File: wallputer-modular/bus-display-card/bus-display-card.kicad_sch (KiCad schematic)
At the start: 1 part

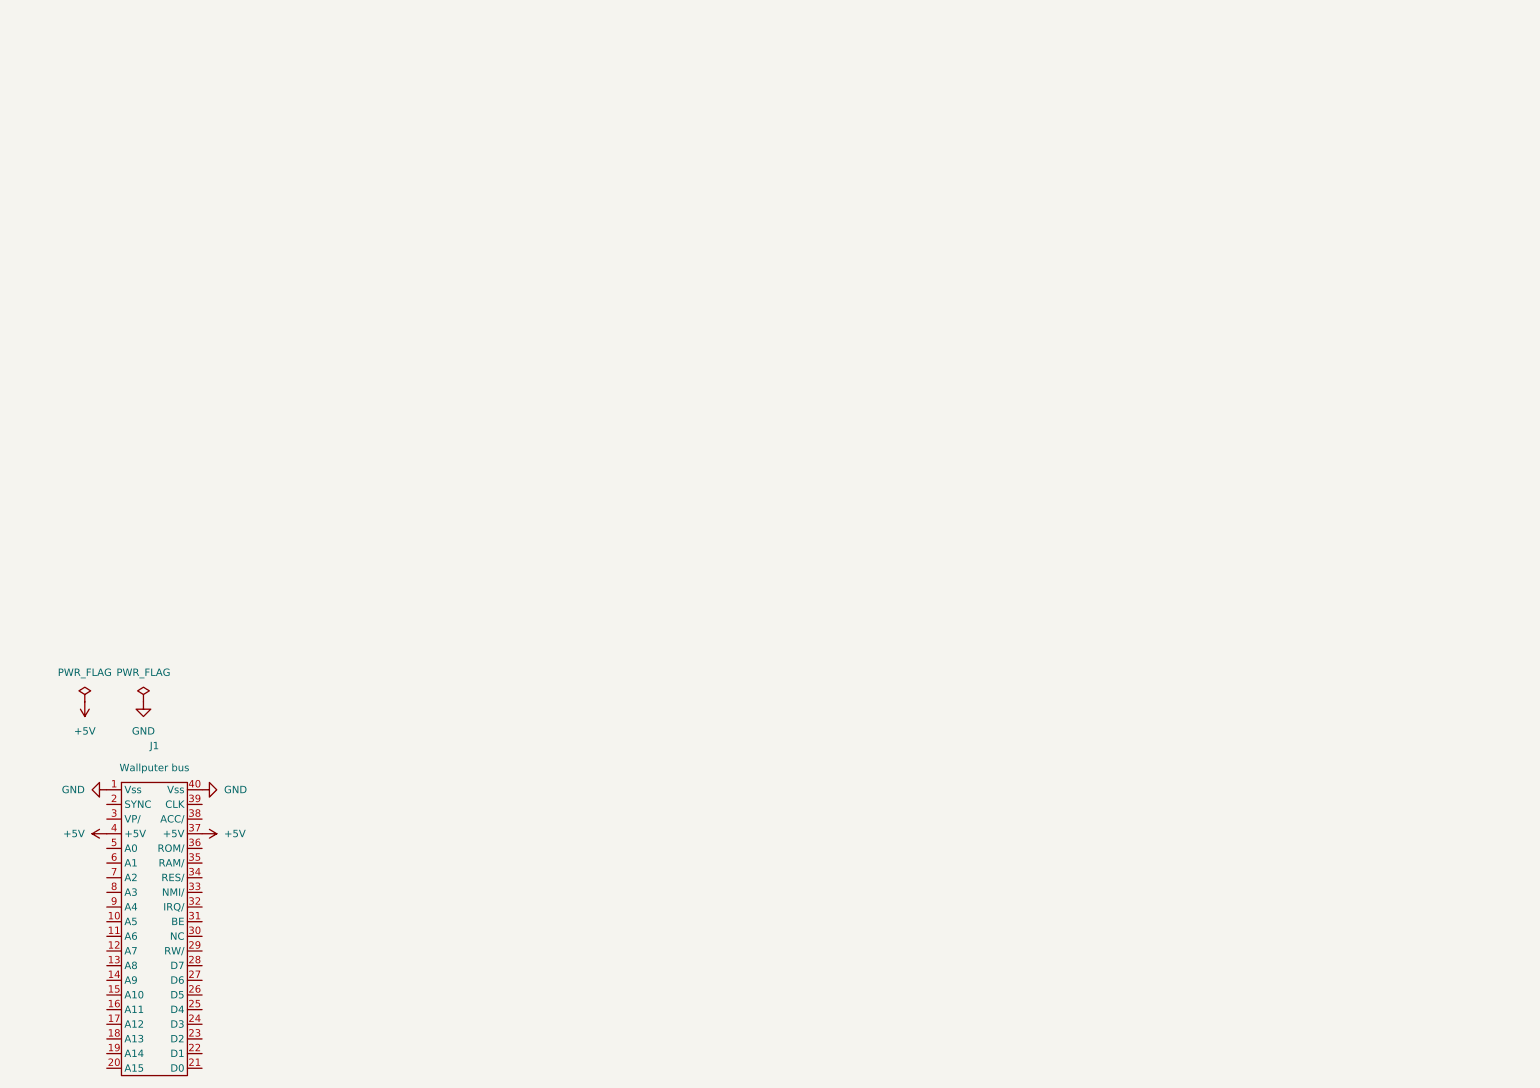
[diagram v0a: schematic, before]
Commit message: copy parts of single board
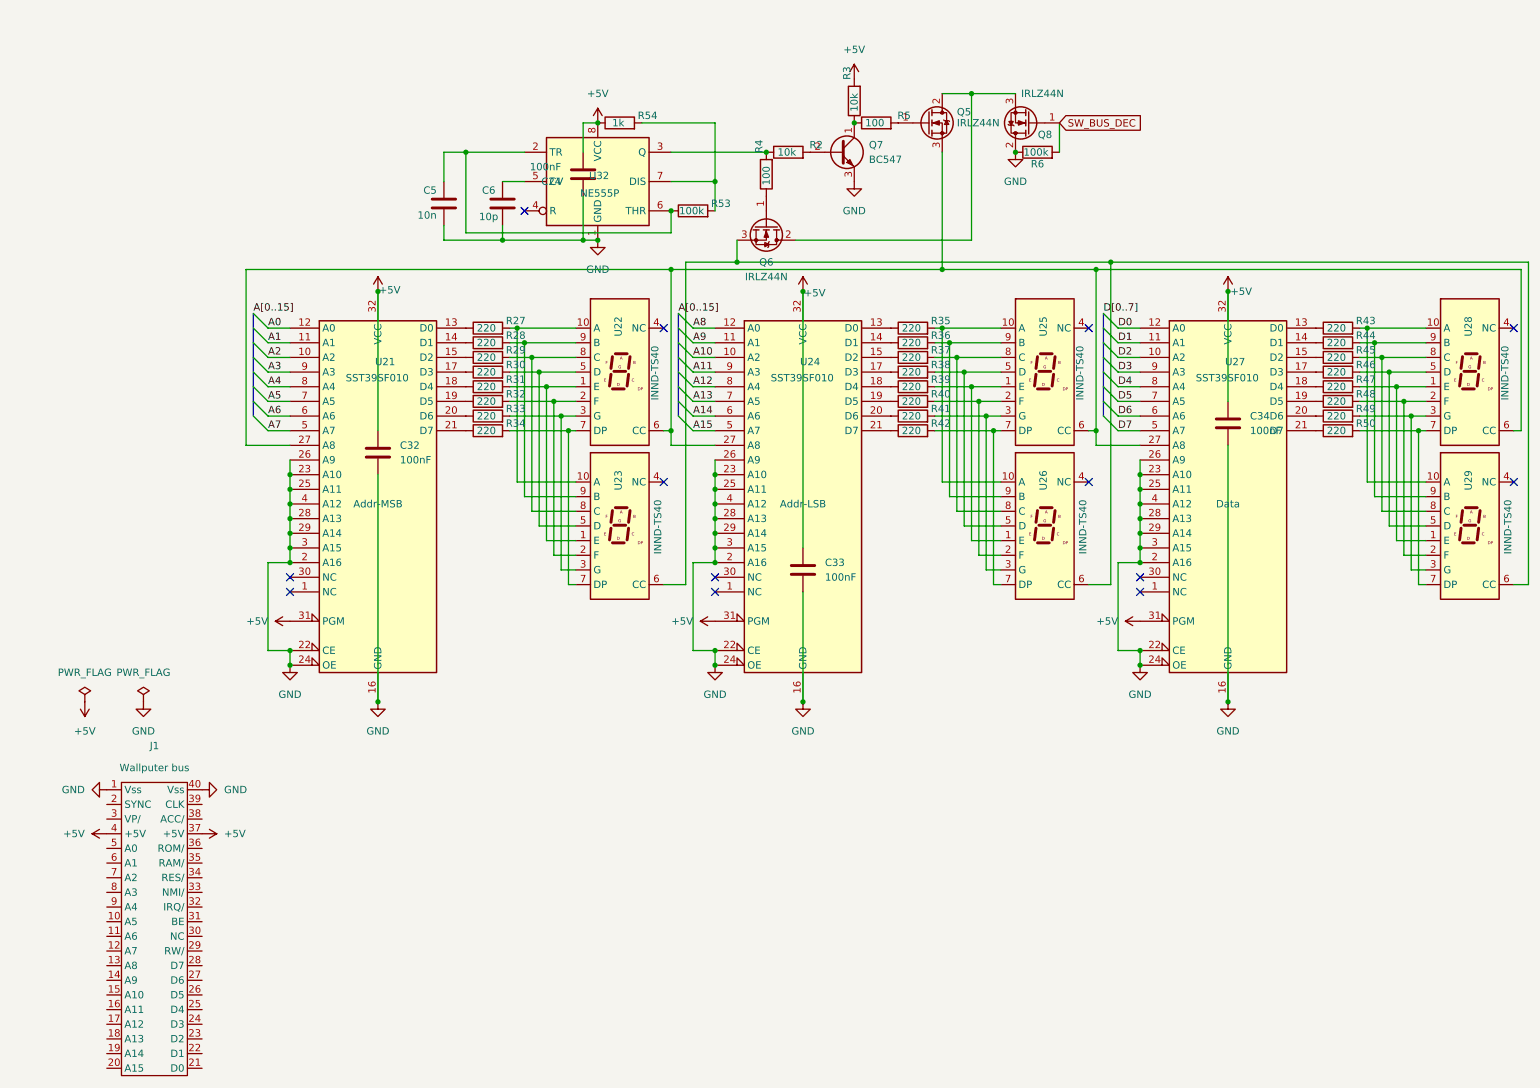
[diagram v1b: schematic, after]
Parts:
- added C24, C32, C33, C34: 100nF, Capacitor_THT:C_Disc_D5.0mm_W2.5mm_P5.00mm, symbol Device:C
- added C5: 10n, Capacitor_THT:C_Disc_D5.0mm_W2.5mm_P5.00mm, symbol Device:C
- added C6: 10p, Capacitor_THT:C_Disc_D5.0mm_W2.5mm_P5.00mm, symbol Device:C
- added Q5, Q6, Q8: IRLZ44N, Package_TO_SOT_THT:TO-220-3_Vertical, symbol Transistor_FET:IRLZ44N
- added Q7: BC547, Package_TO_SOT_THT:TO-92_Inline, symbol Transistor_BJT:BC547
- added R2, R3: 10k, Resistor_THT:R_Axial_DIN0204_L3.6mm_D1.6mm_P2.54mm_Vertical, symbol Device:R
- added R27, R28, R29, R30, R31, R32, R33, R34, R35, R36, R37, R38, R39, R40, R41, R42, R43, R44, R45, R46, R47, R48, R49, R50: 220, Resistor_THT:R_Axial_DIN0204_L3.6mm_D1.6mm_P2.54mm_Vertical, symbol Device:R
- added R4, R5: 100, Resistor_THT:R_Axial_DIN0204_L3.6mm_D1.6mm_P2.54mm_Vertical, symbol Device:R
- added R53, R6: 100k, Resistor_THT:R_Axial_DIN0204_L3.6mm_D1.6mm_P2.54mm_Vertical, symbol Device:R
- added R54: 1k, Resistor_THT:R_Axial_DIN0204_L3.6mm_D1.6mm_P2.54mm_Vertical, symbol Device:R
- added U21, U24, U27: SST39SF010, Package_DIP:DIP-32_W15.24mm_Socket, symbol Memory_Flash:SST39SF010
- added U22, U23, U25, U26, U28, U29: INND-TS40, wallputer:INND-TS40, symbol New_Library:INND-TS40_1
- added U32: NE555P, Package_DIP:DIP-8_W7.62mm, symbol Timer:NE555P
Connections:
- net +5V: now also C24.2, C32.1, C33.1, C34.1, R3.2, R54.1, U21.31 (PGM), U21.32 (VCC), U24.31 (PGM), U24.32 (VCC), U27.31 (PGM), U27.32 (VCC), U32.8 (VCC)
- net GND: now also C24.1, C32.2, C33.2, C34.2, C5.2, C6.2, Q7.3 (E), Q8.2 (D), R6.1, U21.16 (GND), U21.2 (A16), U21.22 (CE), U21.23 (A10), U21.24 (OE), U21.25 (A11), U21.26 (A9), U21.28 (A13), U21.29 (A14), U21.3 (A15), U21.4 (A12), U24.16 (GND), U24.2 (A16), U24.22 (CE), U24.23 (A10), U24.24 (OE), U24.25 (A11), U24.26 (A9), U24.28 (A13), U24.29 (A14), U24.3 (A15), U24.4 (A12), U27.16 (GND), U27.2 (A16), U27.22 (CE), U27.23 (A10), U27.24 (OE), U27.25 (A11), U27.26 (A9), U27.28 (A13), U27.29 (A14), U27.3 (A15), U27.4 (A12), U32.1 (GND)
- new net: R37.1, U24.15 (D2)
- new net: R37.2, U25.8 (C), U26.8 (C)
- new net: R39.2, U25.1 (E), U26.1 (E)
- new net: R35.2, U25.10 (A), U26.10 (A)
- new net: R40.2, U25.2 (F), U26.2 (F)
- new net: R41.2, U25.3 (G), U26.3 (G)
- new net: R38.2, U25.5 (D), U26.5 (D)
- new net: Q5.3 (S), U21.27 (A8), U22.6 (CC), U24.27 (A8), U25.6 (CC), U27.27 (A8), U28.6 (CC)
- new net: R42.2, U25.7 (DP), U26.7 (DP)
- new net: R36.2, U25.9 (B), U26.9 (B)
- new net: R43.1, U27.13 (D0)
- new net: R44.1, U27.14 (D1)
- new net: R45.1, U27.15 (D2)
- new net: R46.1, U27.17 (D3)
- new net: R47.1, U27.18 (D4)
- new net: R48.1, U27.19 (D5)
- new net: R49.1, U27.20 (D6)
- new net: R50.1, U27.21 (D7)
- new net: R33.1, U21.20 (D6)
- new net: R33.2, U22.3 (G), U23.3 (G)
- new net: R38.1, U24.17 (D3)
- new net: R34.1, U21.21 (D7)
- new net: R34.2, U22.7 (DP), U23.7 (DP)
- new net: R47.2, U28.1 (E), U29.1 (E)
- new net: R43.2, U28.10 (A), U29.10 (A)
- new net: R48.2, U28.2 (F), U29.2 (F)
- new net: R49.2, U28.3 (G), U29.3 (G)
- new net: R46.2, U28.5 (D), U29.5 (D)
- new net: R50.2, U28.7 (DP), U29.7 (DP)
- new net: R45.2, U28.8 (C), U29.8 (C)
- new net: R44.2, U28.9 (B), U29.9 (B)
- new net: Q6.1 (G), R4.1
- new net: Q5.2 (D), Q6.2 (D), Q8.3 (S)
- new net: Q6.3 (S), U23.6 (CC), U26.6 (CC), U29.6 (CC)
- new net: R53.2, R54.2, U32.7 (DIS)
- new net: Q7.1 (C), R3.1, R5.1
- new net: Q7.2 (B), R2.2
- new net: R28.1, U21.14 (D1)
- new net: R28.2, U22.9 (B), U23.9 (B)
- new net: R39.1, U24.18 (D4)
- new net: R36.1, U24.14 (D1)
- new net: R2.1, R4.2, U32.3 (Q)
- new net: R31.2, U22.1 (E), U23.1 (E)
- new net: R27.2, U22.10 (A), U23.10 (A)
- new net: R32.2, U22.2 (F), U23.2 (F)
- new net: R30.2, U22.5 (D), U23.5 (D)
- new net: R29.2, U22.8 (C), U23.8 (C)
- new net: R27.1, U21.13 (D0)
- new net: R29.1, U21.15 (D2)
- new net: R30.1, U21.17 (D3)
- new net: R31.1, U21.18 (D4)
- new net: R32.1, U21.19 (D5)
- new net: R35.1, U24.13 (D0)
- new net: R40.1, U24.19 (D5)
- new net: R41.1, U24.20 (D6)
- new net: R42.1, U24.21 (D7)
- new net: Q5.1 (G), R5.2
- new net: C5.1, R53.1, U32.2 (TR), U32.6 (THR)
- new net: C6.1, U32.5 (CV)
- new net A0: U21.12 (A0)
- new net A1: U21.11 (A1)
- new net A10: U24.10 (A2)
- new net A11: U24.9 (A3)
- new net A12: U24.8 (A4)
- new net A13: U24.7 (A5)
- new net A14: U24.6 (A6)
- new net A15: U24.5 (A7)
- new net A2: U21.10 (A2)
- new net A3: U21.9 (A3)
- new net A4: U21.8 (A4)
- new net A5: U21.7 (A5)
- new net A6: U21.6 (A6)
- new net A7: U21.5 (A7)
- new net A8: U24.12 (A0)
- new net A9: U24.11 (A1)
- new net D0: U27.12 (A0)
- new net D1: U27.11 (A1)
- new net D2: U27.10 (A2)
- new net D3: U27.9 (A3)
- new net D4: U27.8 (A4)
- new net D5: U27.7 (A5)
- new net D6: U27.6 (A6)
- new net D7: U27.5 (A7)
- new net SW_BUS_DEC: Q8.1 (G), R6.2
- no-connect marks 0 -> 13

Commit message: bus display PCB
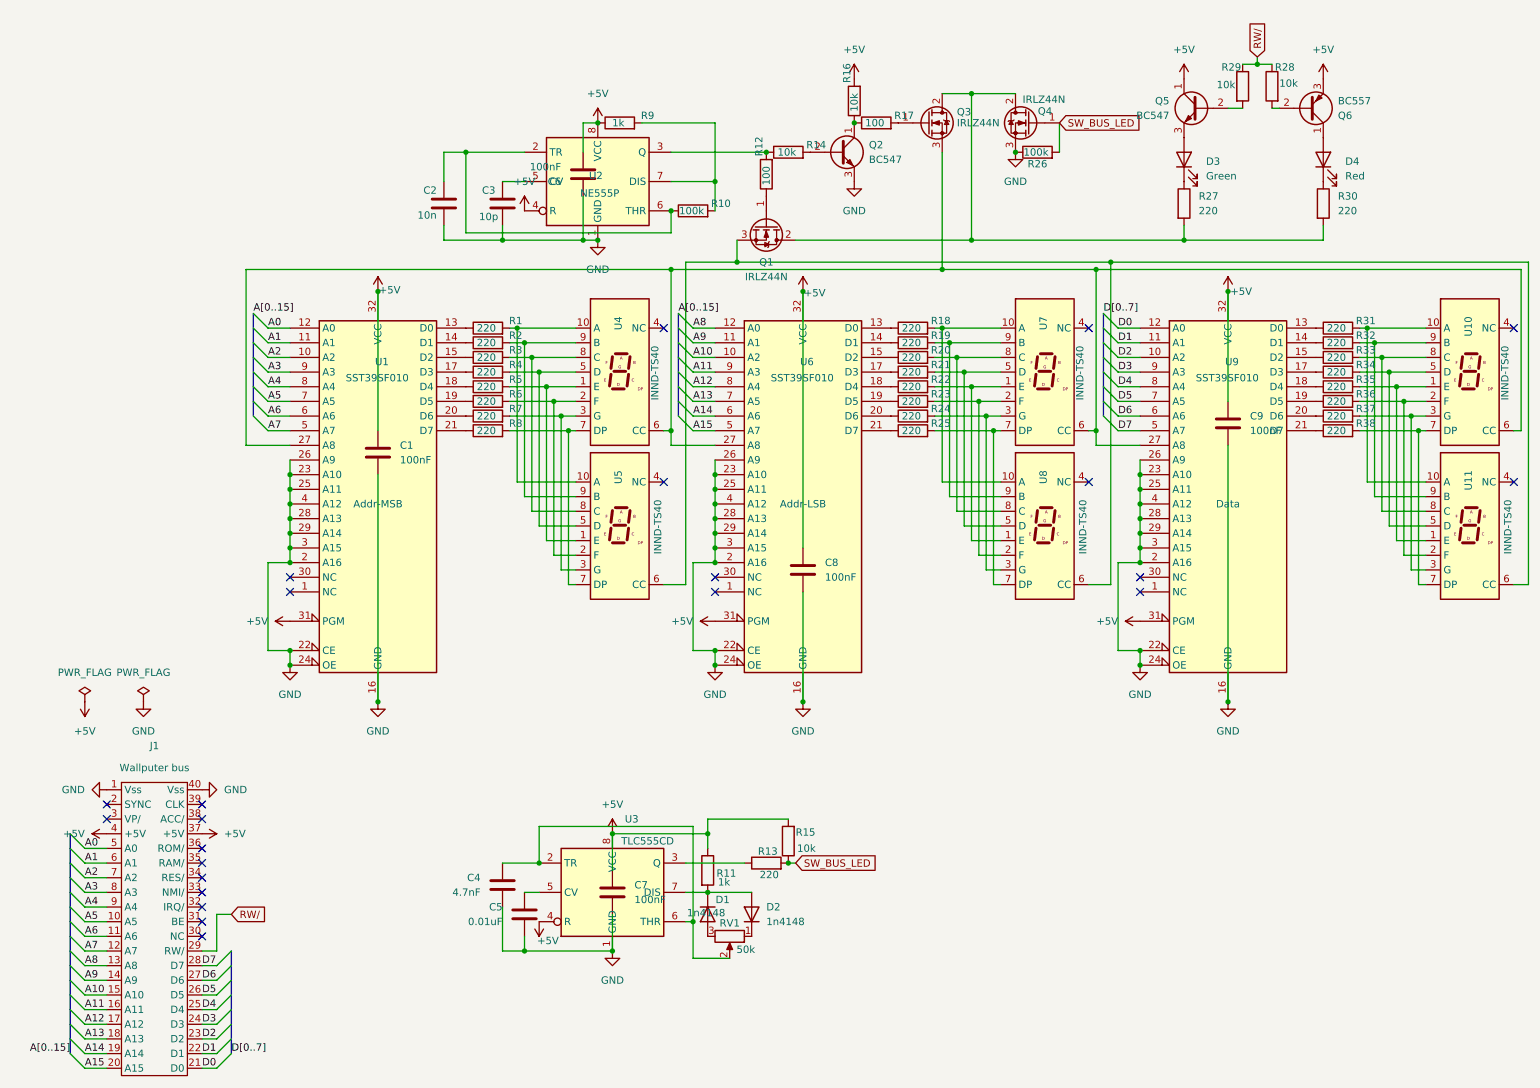
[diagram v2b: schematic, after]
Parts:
- added C4: 4.7nF, Capacitor_THT:C_Disc_D5.0mm_W2.5mm_P5.00mm, symbol Device:C
- added C5: 0.01uF, Capacitor_THT:C_Disc_D5.0mm_W2.5mm_P5.00mm, symbol Device:C
- added C7: 100nF, Capacitor_THT:C_Disc_D5.0mm_W2.5mm_P5.00mm, symbol Device:C
- added D1, D2: 1n4148, Diode_THT:D_DO-35_SOD27_P7.62mm_Horizontal, symbol Device:D
- added D3: Green, LED_THT:LED_D3.0mm, symbol Device:LED
- added D4: Red, LED_THT:LED_D3.0mm, symbol Device:LED
- added Q5: BC547, Package_TO_SOT_THT:TO-92_Inline, symbol Transistor_BJT:BC547
- added Q6: BC557, Package_TO_SOT_THT:TO-92_Inline, symbol Transistor_BJT:BC557
- added R11: 1k, Resistor_THT:R_Axial_DIN0204_L3.6mm_D1.6mm_P2.54mm_Vertical, symbol Device:R
- added R13, R27, R30: 220, Resistor_THT:R_Axial_DIN0204_L3.6mm_D1.6mm_P2.54mm_Vertical, symbol Device:R
- added R15, R28, R29: 10k, Resistor_THT:R_Axial_DIN0204_L3.6mm_D1.6mm_P2.54mm_Vertical, symbol Device:R
- added RV1: 50k, Potentiometer_THT:Potentiometer_Alpha_RD901F-40-00D_Single_Vertical, symbol Device:R_Potentiometer
- added U3: TLC555CD, Package_DIP:DIP-8_W7.62mm, symbol Timer:NE555P
- U10: renamed from U28; footprint wallputer:INND-TS40 -> Wallputer:INND-TS40; symbol New_Library:INND-TS40_1 -> wallputer:INND-TS40_1
- U11: renamed from U29; footprint wallputer:INND-TS40 -> Wallputer:INND-TS40; symbol New_Library:INND-TS40_1 -> wallputer:INND-TS40_1
- U4: renamed from U22; footprint wallputer:INND-TS40 -> Wallputer:INND-TS40; symbol New_Library:INND-TS40_1 -> wallputer:INND-TS40_1
- U5: renamed from U23; footprint wallputer:INND-TS40 -> Wallputer:INND-TS40; symbol New_Library:INND-TS40_1 -> wallputer:INND-TS40_1
- U7: renamed from U25; footprint wallputer:INND-TS40 -> Wallputer:INND-TS40; symbol New_Library:INND-TS40_1 -> wallputer:INND-TS40_1
- U8: renamed from U26; footprint wallputer:INND-TS40 -> Wallputer:INND-TS40; symbol New_Library:INND-TS40_1 -> wallputer:INND-TS40_1
- renumbered C32 to C1, C5 to C2, C6 to C3, C24 to C6, C33 to C8, C34 to C9, Q6 to Q1, Q7 to Q2, Q5 to Q3, Q8 to Q4, R27 to R1, R53 to R10, R4 to R12, R2 to R14, R3 to R16, R5 to R17, R35 to R18, R36 to R19, R28 to R2, R37 to R20, R38 to R21, R39 to R22, R40 to R23, R41 to R24, R42 to R25, R6 to R26, R29 to R3, R43 to R31, R44 to R32, R45 to R33, R46 to R34, R47 to R35, R48 to R36, R49 to R37, R50 to R38, R30 to R4, R31 to R5, R32 to R6, R33 to R7, R34 to R8, R54 to R9, U21 to U1, U32 to U2, U24 to U6, U27 to U9
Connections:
- net +5V: now also U2.4 (R), C7.1, Q5.1 (C), Q6.3 (E), R11.1, R15.2, U3.4 (R), U3.8 (VCC)
- net A0: now also J1.5 (A0)
- net A1: now also J1.6 (A1)
- net A10: now also J1.15 (A10)
- net A11: now also J1.16 (A11)
- net A12: now also J1.17 (A12)
- net A13: now also J1.18 (A13)
- net A14: now also J1.19 (A14)
- net A15: now also J1.20 (A15)
- net A2: now also J1.7 (A2)
- net A3: now also J1.8 (A3)
- net A4: now also J1.9 (A4)
- net A5: now also J1.10 (A5)
- net A6: now also J1.11 (A6)
- net A7: now also J1.12 (A7)
- net A8: now also J1.13 (A8)
- net A9: now also J1.14 (A9)
- net D0: now also J1.21 (D0)
- net D1: now also J1.22 (D1)
- net D2: now also J1.23 (D2)
- net D3: now also J1.24 (D3)
- net D4: now also J1.25 (D4)
- net D5: now also J1.26 (D5)
- net D6: now also J1.27 (D6)
- net D7: now also J1.28 (D7)
- net GND: now also Q4.3 (S), C4.2, C5.1, C7.2, U3.1 (GND); no longer Q4.2 (D)
- net RW/: now reaches J1.29 (RW/)
- net RW/: now also R28.1, R29.1
- net at Q1.2 (D), Q3.2 (D): now also Q4.2 (D), R27.2, R30.2; no longer Q4.3 (S)
- net SW_BUS_DEC renamed SW_BUS_LED
- net SW_BUS_LED: now also R13.2, R15.1
- new net: C4.1, RV1.2, U3.2 (TR), U3.6 (THR)
- new net: Q6.2 (B), R29.2
- new net: D4.2 (A), Q6.1 (C)
- new net: Q5.2 (B), R28.2
- new net: D3.2 (A), Q5.3 (E)
- new net: D4.1 (K), R30.1
- new net: D1.1 (K), D2.2 (A), R11.2, U3.7 (DIS)
- new net: D1.2 (A), RV1.3
- new net: D3.1 (K), R27.1
- new net: C5.2, U3.5 (CV)
- new net: R13.1, U3.3 (Q)
- new net: D2.1 (K), RV1.1
- no-connect marks 13 -> 23
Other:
- moved on the sheet: Q4
